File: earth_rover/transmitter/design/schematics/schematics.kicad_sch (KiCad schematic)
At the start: 6 parts, among them U3 XIAO-ESP32-C3-DIP

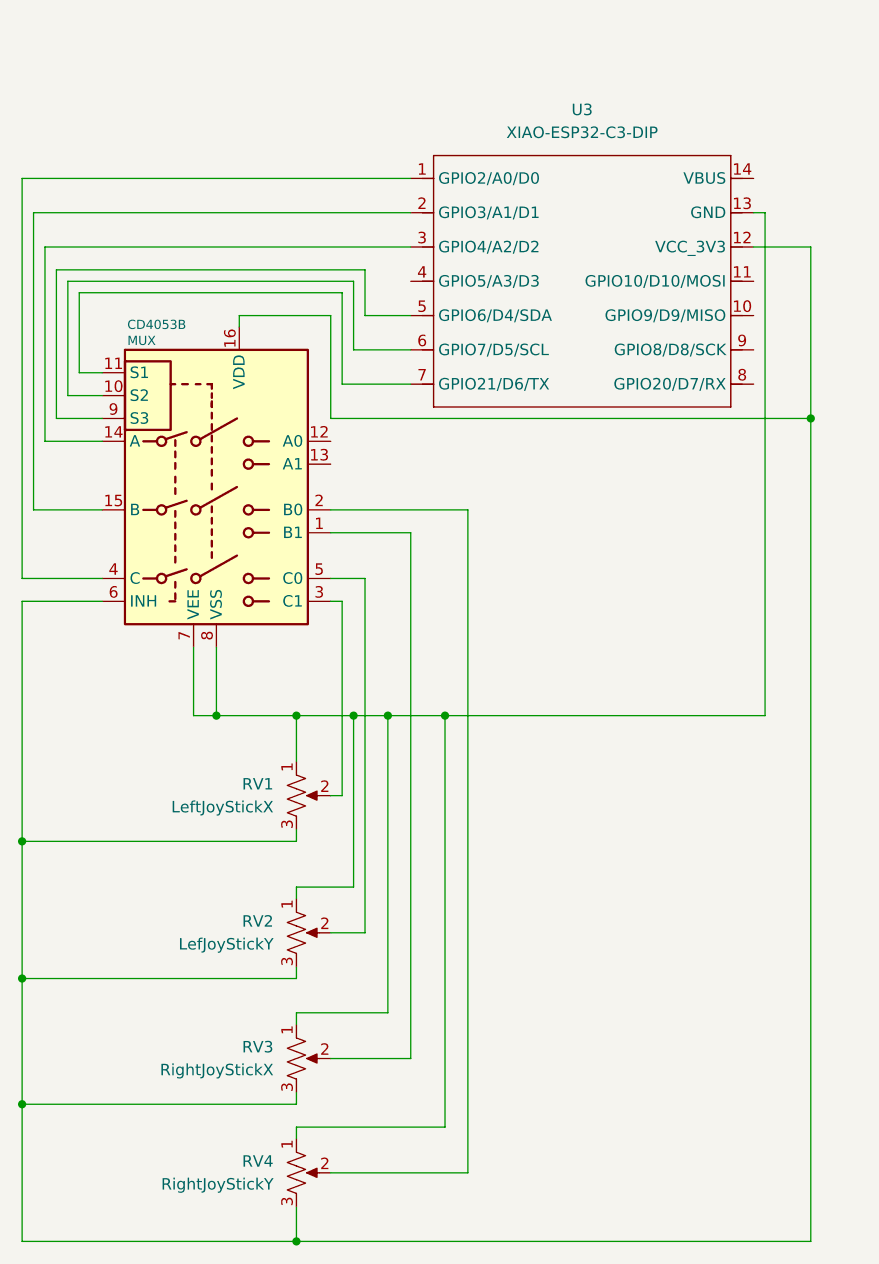
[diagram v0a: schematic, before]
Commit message: Revision 1.0.2 - Transmitter Schematic
- Adds disconnected markers
- Fixes INH line
- Adds better EPS32C3 Symbol
- Disconnects an unused output
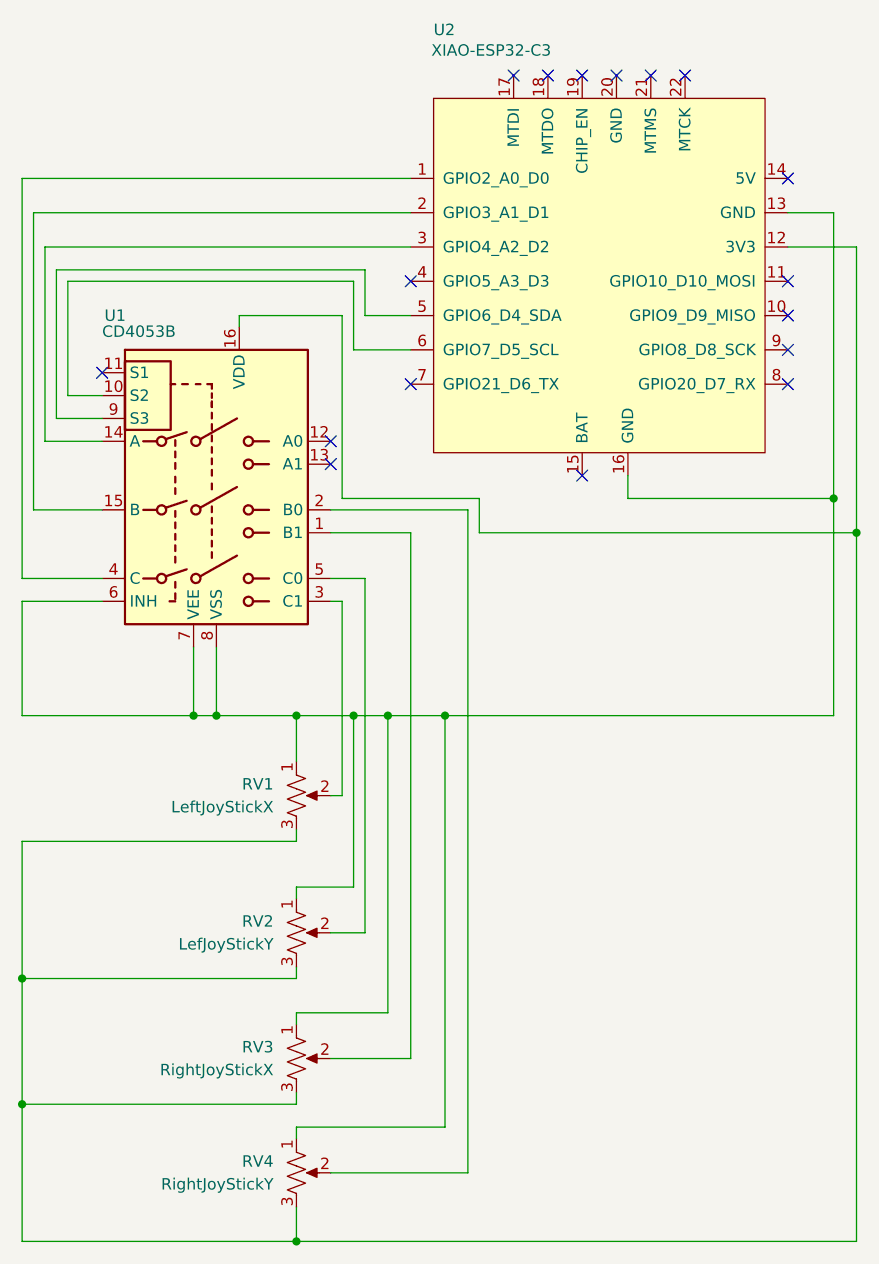
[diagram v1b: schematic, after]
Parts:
- removed U3: XIAO-ESP32-C3-DIP, Module:MOUDLE14P-XIAO-DIP-SMD, symbol Seeed_Studio_XIAO_Series:XIAO-ESP32-C3-DIP
- added U2: XIAO-ESP32-C3, symbol Seeed_Studio_XIAO_Series:XIAO-ESP32-C3-SMD
- renumbered MUX to U1
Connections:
- net at RV1.1, RV2.1, RV3.1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: now also U1.6 (INH), U2.13 (GND), U2.16 (GND)
- net at RV1.3, RV2.3, RV3.3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: now also U2.12 (3V3); no longer U1.6 (INH)
- net at U1.10 (S2): now also U2.6 (GPIO7_D5_SCL)
- net at U1.14 (A): now also U2.3 (GPIO4_A2_D2)
- net at U1.15 (B): now also U2.2 (GPIO3_A1_D1)
- net at U1.4 (C): now also U2.1 (GPIO2_A0_D0)
- net at U1.9 (S3): now also U2.5 (GPIO6_D4_SDA)
- no-connect marks 0 -> 17
